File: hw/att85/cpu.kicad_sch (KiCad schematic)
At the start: 10 parts, among them J201 Conn_01x06, U201 STM32G030K8Tx, U202 74AHCT125

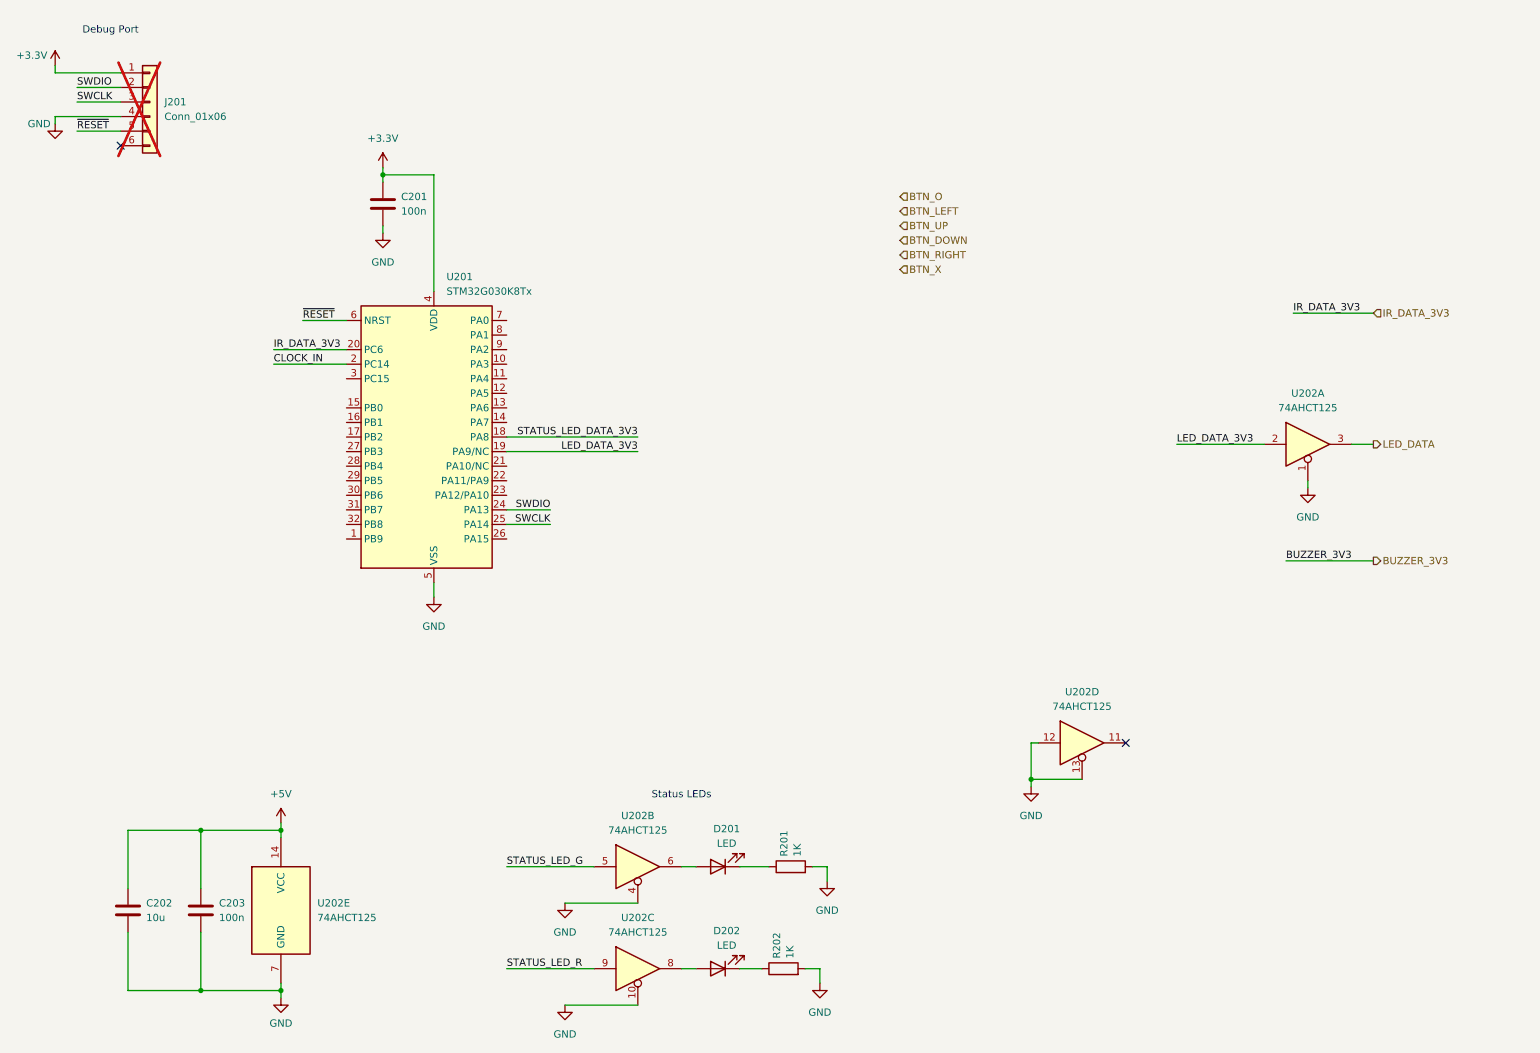
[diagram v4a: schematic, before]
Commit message: chore(hw): add peripheral connections, layout power supply
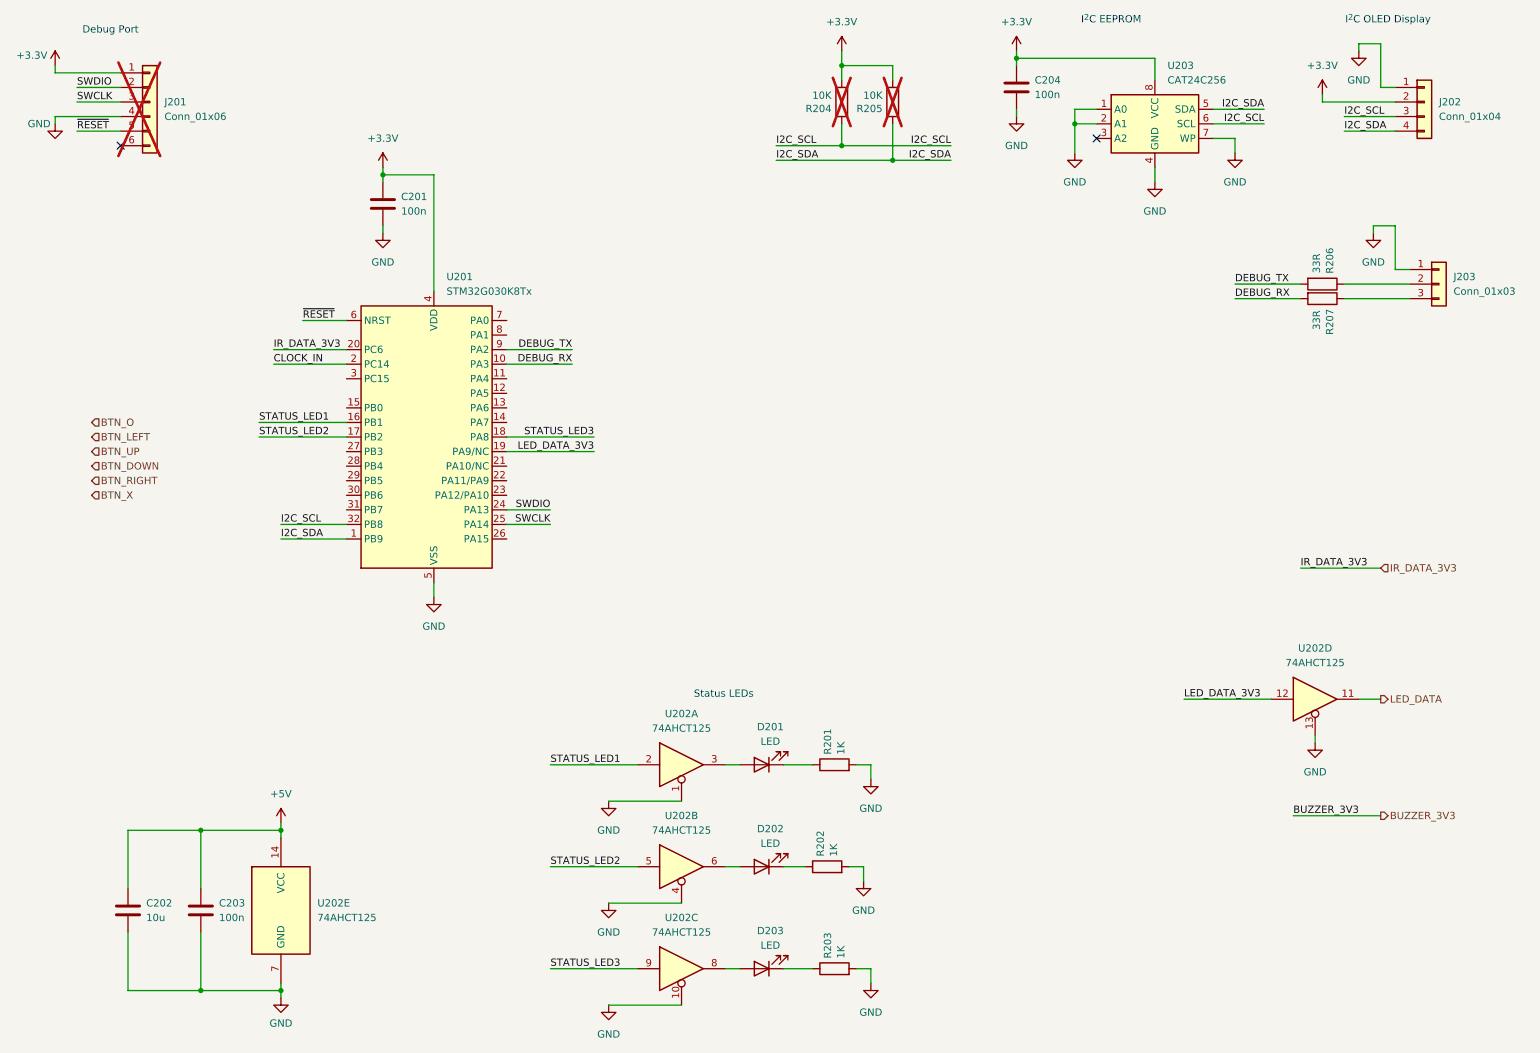
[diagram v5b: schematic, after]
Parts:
- added C204: 100n, Capacitor_SMD:C_0805_2012Metric_Pad1.18x1.45mm_HandSolder, symbol Device:C
- added D203: LED, LED_SMD:LED_0805_2012Metric_Pad1.15x1.40mm_HandSolder, symbol Device:LED
- added J202: Conn_01x04, Connector_PinSocket_2.54mm:PinSocket_1x04_P2.54mm_Vertical, symbol Connector_Generic:Conn_01x04
- added J203: Conn_01x03, Connector_PinHeader_2.54mm:PinHeader_1x03_P2.54mm_Vertical, symbol Connector_Generic:Conn_01x03
- added R203: 1K, Resistor_SMD:R_0805_2012Metric_Pad1.20x1.40mm_HandSolder, symbol Device:R
- added R204, R205: 10K, Resistor_SMD:R_0805_2012Metric_Pad1.20x1.40mm_HandSolder, symbol Device:R
- added R206, R207: 33R, Resistor_SMD:R_0805_2012Metric_Pad1.20x1.40mm_HandSolder, symbol Device:R
- added U203: CAT24C256, Package_DIP:DIP-8_W7.62mm_Socket, symbol Memory_EEPROM:CAT24C256
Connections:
- net STATUS_LED_G is gone; now on net STATUS_LED2: U202.5
- net STATUS_LED_R is gone; now on net STATUS_LED3: U202.9
- net +3.3V: now also C204.1, J202.2 (Pin_2), R204.2, R205.2, U203.8 (VCC)
- net GND: now also C204.2, J202.1 (Pin_1), J203.1 (Pin_1), R203.2, U203.1 (A0), U203.2 (A1), U203.4 (GND), U203.7 (WP); no longer U202.12
- net LED_DATA: now also U202.11; no longer U202.3
- net LED_DATA_3V3: now also U202.12; no longer U202.2
- net I2C_SDA: now reaches U201.1 (PB9)
- net I2C_SDA: now also J202.4 (Pin_4), R205.1, U203.5 (SDA)
- net DEBUG_RX: now reaches U201.10 (PA3)
- net DEBUG_RX: now also R207.2
- net STATUS_LED1: now reaches U201.16 (PB1)
- net STATUS_LED1: now also U202.2
- net STATUS_LED2: now reaches U201.17 (PB2)
- net I2C_SCL: now reaches U201.32 (PB8)
- net I2C_SCL: now also J202.3 (Pin_3), R204.1, U203.6 (SCL)
- net DEBUG_TX: now reaches U201.9 (PA2)
- net DEBUG_TX: now also R206.2
- net at D202.2 (A): now also U202.6; no longer U202.8
- net at D201.2 (A): now also U202.3; no longer U202.6
- net STATUS_LED_DATA_3V3 renamed STATUS_LED3
- new net: D203.1 (K), R203.1
- new net: D203.2 (A), U202.8
- new net: J203.3 (Pin_3), R207.1
- new net: J203.2 (Pin_2), R206.1
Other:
- note added: "I^{2}C EEPROM"
- note added: "I^{2}C OLED Display"
- moved on the sheet: D201, D202, R201, R202, U202A, U202B, U202C, U202D

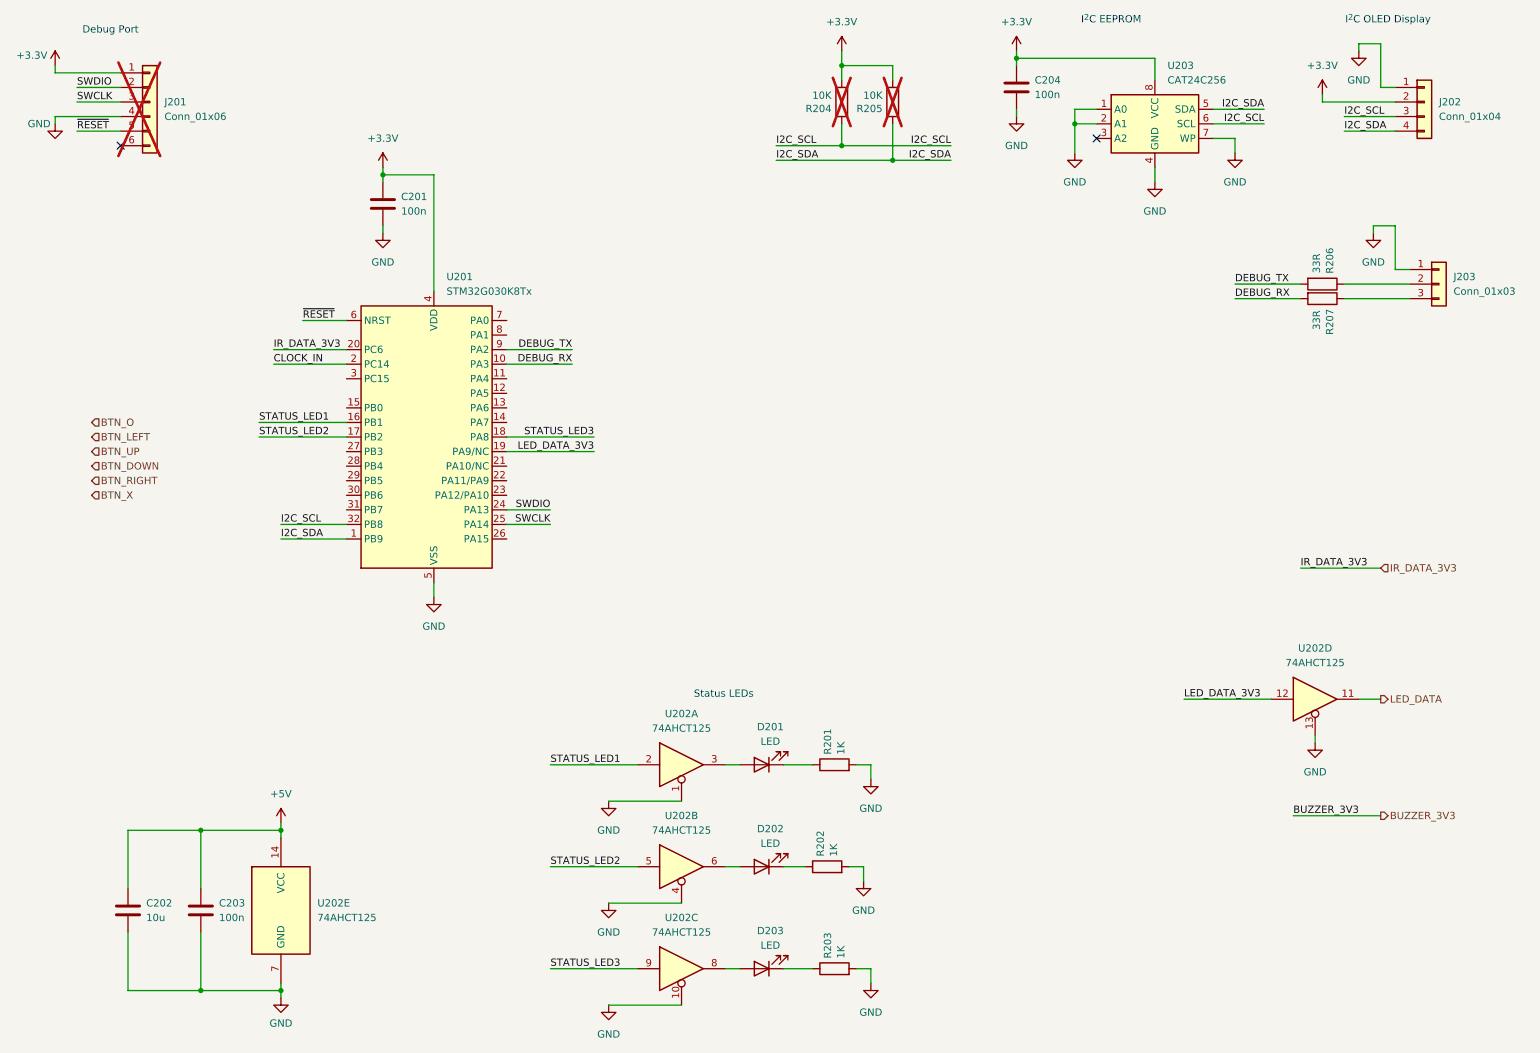
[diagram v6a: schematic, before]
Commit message: chore(hw): add buzzer connection
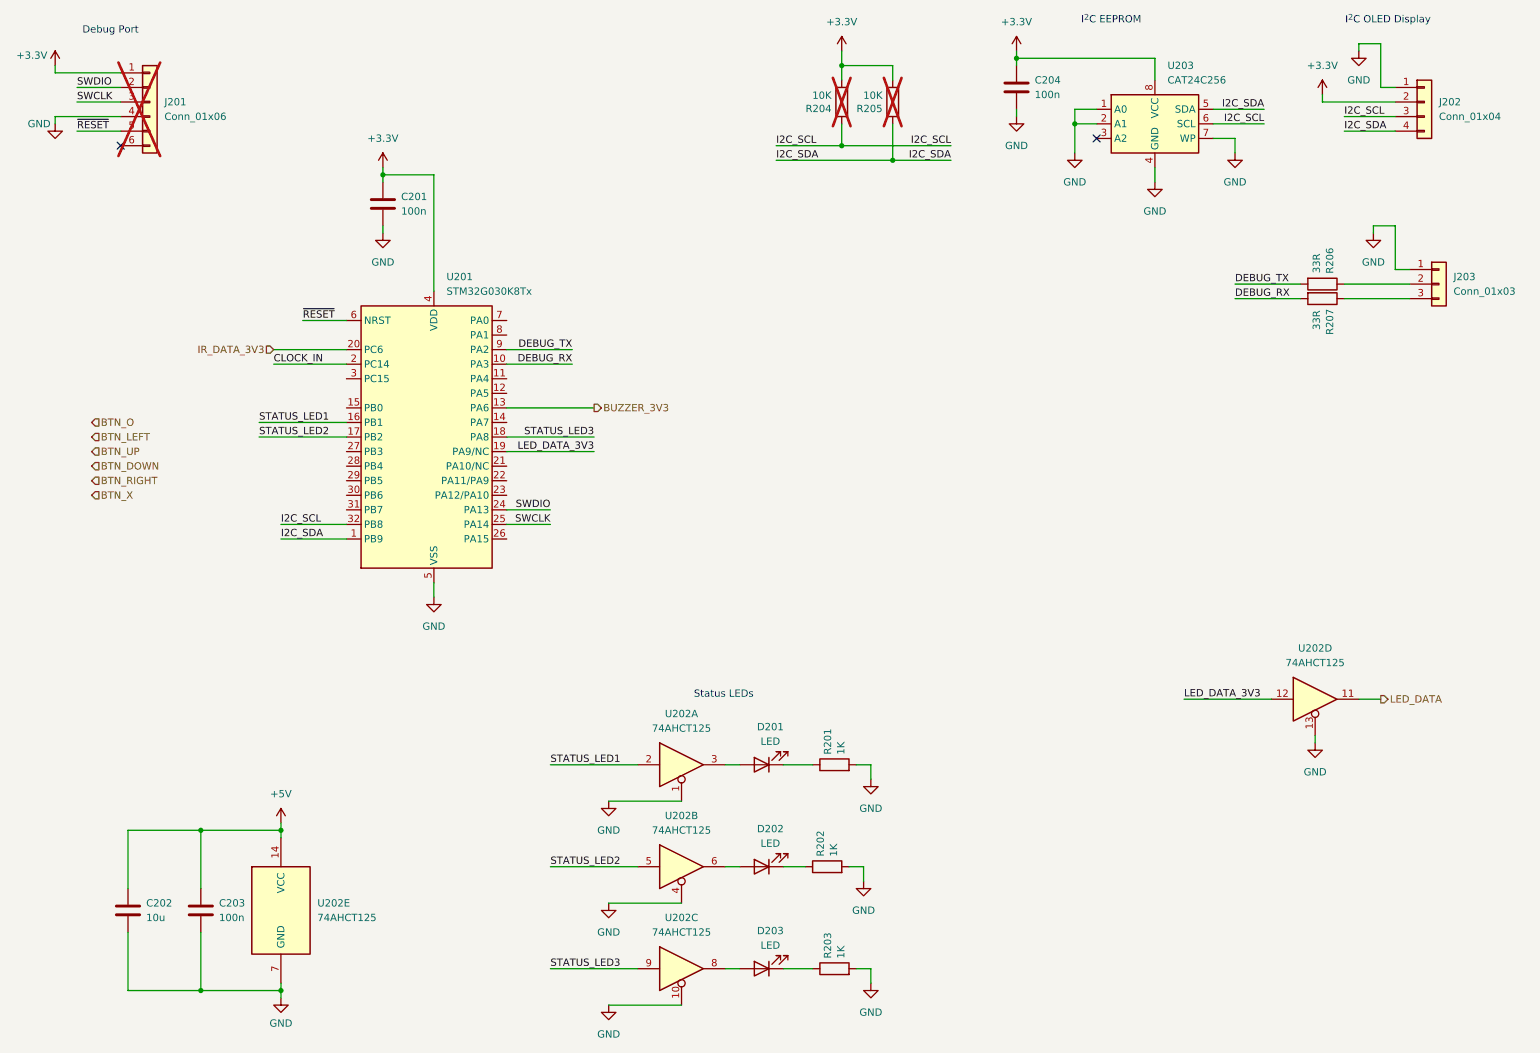
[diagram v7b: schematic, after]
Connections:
- net BUZZER_3V3: now also U201.13 (PA6)
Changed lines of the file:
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@@
-	(wire
-		(pts
-			(xy 243.84 157.48) (xy 259.08 157.48)
-		)
-		(stroke
-			(width 0)
-			(type default)
-		)
-	)
 	(wire
 		(pts
@@
 	(wire
 		(pts
-			(xy 245.11 114.3) (xy 259.08 114.3)
-		)
-		(stroke
-			(width 0)
-			(type default)
-		)
-	)
-	(wire
-		(pts
 			(xy 195.58 25.4) (xy 219.71 25.4)
 		)
@@
 		(pts
 			(xy 27.94 27.94) (xy 39.37 27.94)
+		)
+		(stroke
+			(width 0)
+			(type default)
+		)
+	)
+	(wire
+		(pts
+			(xy 106.68 86.36) (xy 121.92 86.36)
 		)
 		(stroke
@@
 		)
 	)
-	(label "IR_DATA_3V3"
-		(at 245.11 114.3 0)
-		(fields_autoplaced yes)
-		(effects
-			(font
-				(size 1.27 1.27)
-			)
-			(justify left bottom)
-		)
-	)
 	(label "I2C_SCL"
 		(at 184.15 40.64 180)
@@
 		)
 	)
-	(label "IR_DATA_3V3"
-		(at 66.04 76.2 0)
-		(fields_autoplaced yes)
-		(effects
-			(font
-				(size 1.27 1.27)
-			)
-			(justify left bottom)
-		)
-	)
 	(label "~{RESET}"
 		(at 71.12 71.12 0)
@@
 	(label "SWDIO"
 		(at 31.75 30.48 0)
-		(fields_autoplaced yes)
-		(effects
-			(font
-				(size 1.27 1.27)
-			)
-			(justify left bottom)
-		)
-	)
-	(label "BUZZER_3V3"
-		(at 243.84 157.48 0)
 		(fields_autoplaced yes)
 		(effects
@@
 	(hierarchical_label "IR_DATA_3V3"
 		(shape input)
-		(at 259.08 114.3 0)
-		(fields_autoplaced yes)
-		(effects
-			(font
-				(size 1.27 1.27)
-			)
-			(justify left)
+		(at 66.04 76.2 180)
+		(fields_autoplaced yes)
+		(effects
+			(font
+				(size 1.27 1.27)
+			)
+			(justify right)
 		)
 	)
@@
 	(hierarchical_label "BUZZER_3V3"
 		(shape output)
-		(at 259.08 157.48 0)
-		(fields_autoplaced yes)
-		(effects
+		(at 121.92 86.36 0)
+		(fields_autoplaced yes)
+		(effects

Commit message: chore(hw): partial layout
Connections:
- net BTN_DOWN: now also U201.28 (PB4)
- net BTN_LEFT: now also U201.27 (PB3)
- net BTN_O: now also U201.26 (PA15)
- net BTN_RIGHT: now also U201.29 (PB5)
- net BTN_UP: now also U201.31 (PB7)
- net BTN_X: now also U201.30 (PB6)
- no-connect marks 2 -> 13
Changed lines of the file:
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@@
+	)
+	(no_connect
+		(at 106.68 83.82)
+	)
+	(no_connect
+		(at 78.74 86.36)
+	)
+	(no_connect
+		(at 66.04 78.74)
+	)
+	(no_connect
+		(at 106.68 101.6)
+	)
+	(no_connect
+		(at 106.68 73.66)
+	)
+	(no_connect
+		(at 106.68 99.06)
+	)
+	(no_connect
+		(at 106.68 71.12)
 	)
 	(no_connect
@@
 		(at 39.37 40.64)
 	)
+	(no_connect
+		(at 106.68 88.9)
+	)
+	(no_connect
+		(at 78.74 81.28)
+	)
+	(no_connect
+		(at 106.68 96.52)
+	)
+	(no_connect
+		(at 106.68 81.28)
+	)
 	(wire
 		(pts
@@
 	(wire
 		(pts
+			(xy 63.5 101.6) (xy 78.74 101.6)
+		)
+		(stroke
+			(width 0)
+			(type default)
+		)
+	)
+	(wire
+		(pts
 			(xy 259.08 22.86) (xy 255.27 22.86)
 		)
@@
 	(wire
 		(pts
+			(xy 63.5 104.14) (xy 78.74 104.14)
+		)
+		(stroke
+			(width 0)
+			(type default)
+		)
+	)
+	(wire
+		(pts
 			(xy 39.37 33.02) (xy 31.75 33.02)
 		)
@@
 	(wire
 		(pts
+			(xy 63.5 96.52) (xy 78.74 96.52)
+		)
+		(stroke
+			(width 0)
+			(type default)
+		)
+	)
+	(wire
+		(pts
 			(xy 106.68 86.36) (xy 121.92 86.36)
 		)
@@
 	(wire
 		(pts
+			(xy 114.3 109.22) (xy 106.68 109.22)
+		)
+		(stroke
+			(width 0)
+			(type default)
+		)
+	)
+	(wire
+		(pts
 			(xy 165.1 40.64) (xy 184.15 40.64)
 		)
@@
 	(wire
 		(pts
+			(xy 63.5 99.06) (xy 78.74 99.06)
+		)
+		(stroke
+			(width 0)
+			(type default)
+		)
+	)
+	(wire
+		(pts
 			(xy 165.1 24.13) (xy 165.1 26.67)
 		)
@@
 		(pts
 			(xy 154.94 148.59) (xy 160.02 148.59)
+		)
+		(stroke
+			(width 0)
+			(type default)
+		)
+	)
+	(wire
+		(pts
+			(xy 63.5 93.98) (xy 78.74 93.98)
 		)
 		(stroke
@@
 	(hierarchical_label "BTN_X"
 		(shape input)
-		(at 34.29 101.6 0)
-		(fields_autoplaced yes)
-		(effects
-			(font
-				(size 1.27 1.27)
-			)
-			(justify left)
+		(at 63.5 101.6 180)
+		(fields_autoplaced yes)
+		(effects
+			(font
+				(size 1.27 1.27)
+			)
+			(justify right)
 		)
 	)
 	(hierarchical_label "BTN_RIGHT"
 		(shape input)
-		(at 34.29 99.06 0)
-		(fields_autoplaced yes)
-		(effects
-			(font
-				(size 1.27 1.27)
-			)
-			(justify left)
+		(at 63.5 99.06 180)
+		(fields_autoplaced yes)
+		(effects
+			(font
+				(size 1.27 1.27)
+			)
+			(justify right)
 		)
 	)
@@
 	(hierarchical_label "BTN_LEFT"
 		(shape input)
-		(at 34.29 91.44 0)
-		(fields_autoplaced yes)
-		(effects
-			(font
-				(size 1.27 1.27)
-			)
-			(justify left)
+		(at 63.5 93.98 180)
+		(fields_autoplaced yes)
+		(effects
+			(font
+				(size 1.27 1.27)
+			)
+			(justify right)
 		)
 	)
 	(hierarchical_label "BTN_UP"
 		(shape input)
-		(at 34.29 93.98 0)
-		(fields_autoplaced yes)
-		(effects
-			(font
-				(size 1.27 1.27)
-			)
-			(justify left)
+		(at 63.5 104.14 180)
+		(fields_autoplaced yes)
+		(effects
+			(font
+				(size 1.27 1.27)
+			)
+			(justify right)
 		)
 	)
@@
 	(hierarchical_label "BTN_O"
 		(shape input)
-		(at 34.29 88.9 0)
+		(at 114.3 109.22 0)
 		(fields_autoplaced yes)
 		(effects
@@
 	(hierarchical_label "BTN_DOWN"
 		(shape input)
-		(at 34.29 96.52 0)
-		(fields_autoplaced yes)
-		(effects
-			(font
-				(size 1.27 1.27)
-			)
-			(justify left)
-		)
-	)
+		(at 63.5 96.52 180)
+		(fields_autoplaced yes)
+		(effects
+			(font
+				(size 1.27 1.27)
+			)
+			(justify right)
+		)
+	)
